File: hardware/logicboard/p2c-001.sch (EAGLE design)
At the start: 45 parts, among them IC1 74LS07N, K1 G5V1, T1 2SC1815

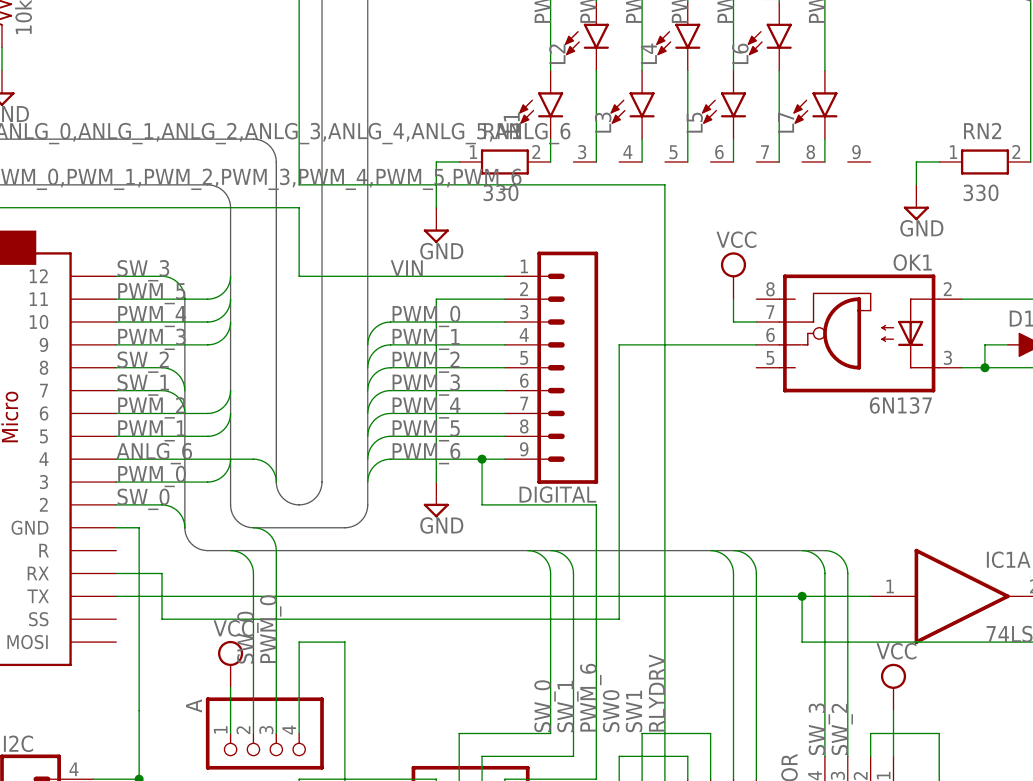
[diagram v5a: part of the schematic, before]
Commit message: Added RCV LED.
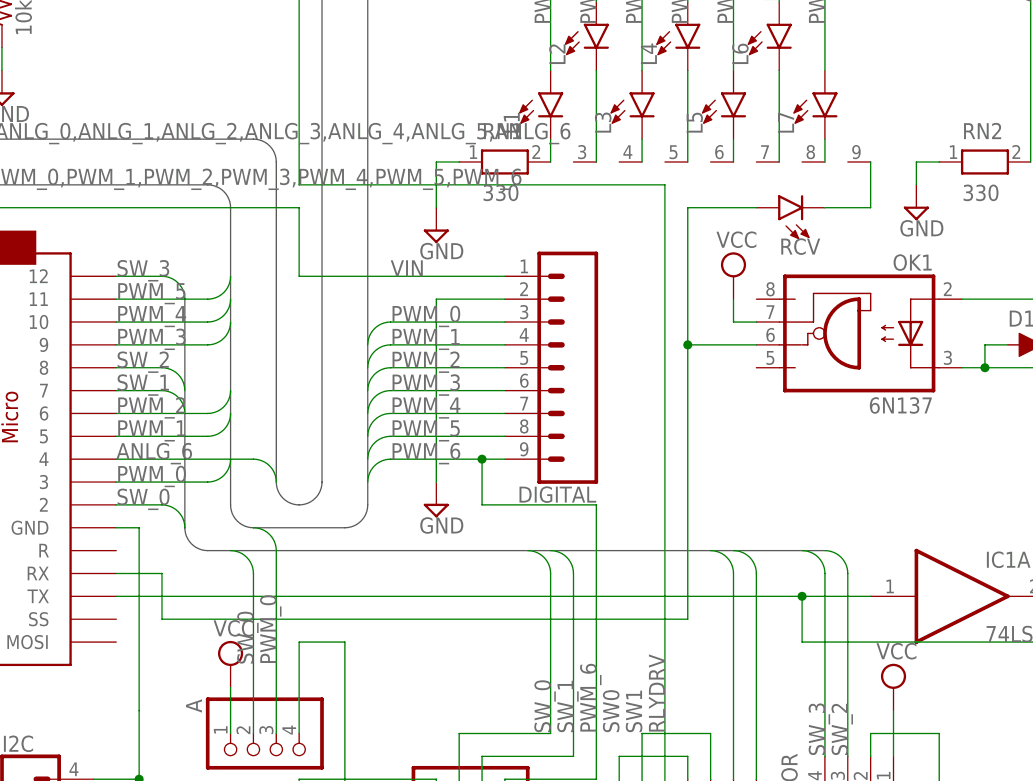
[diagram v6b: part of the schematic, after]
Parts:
- added RCV: (no value), SparkFun-LED:LED-3MM-NO_SILK
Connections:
- new net N$1: RCV.C, RN1.9
- net MIDIIN: now also RCV.A
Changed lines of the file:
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@@
 <part name="XOUT" library="SparkFun-Connectors" library_urn="urn:adsk.eagle:library:513" deviceset="CONN_05" device="" package3d_urn="urn:adsk.eagle:package:38104/1"/>
 <part name="U$3" library="pineapple" deviceset="KANAYA768_SILK" device=""/>
+<part name="RCV" library="SparkFun-LED" deviceset="LED" device="-3MM-NO_SILK"/>
 </parts>
 <sheets>
@@
 <instance part="XOUT" gate="G$1" x="236.22" y="111.76" rot="MR180"/>
 <instance part="U$3" gate="G$1" x="187.96" y="5.08"/>
+<instance part="RCV" gate="G$1" x="142.24" y="99.06" rot="R90"/>
 </instances>
 <busses>
@@
 <segment>
 <pinref part="OK1" gate="A" pin="VO"/>
-<wire x1="139.7" y1="83.82" x2="124.46" y2="83.82" width="0.1524" layer="91"/>
+<wire x1="139.7" y1="83.82" x2="132.08" y2="83.82" width="0.1524" layer="91"/>
 <pinref part="U$2" gate="G$1" pin="RX"/>
-<wire x1="124.46" y1="83.82" x2="124.46" y2="53.34" width="0.1524" layer="91"/>
-<wire x1="124.46" y1="53.34" x2="73.66" y2="53.34" width="0.1524" layer="91"/>
+<wire x1="132.08" y1="83.82" x2="132.08" y2="53.34" width="0.1524" layer="91"/>
+<wire x1="132.08" y1="53.34" x2="73.66" y2="53.34" width="0.1524" layer="91"/>
 <wire x1="73.66" y1="53.34" x2="73.66" y2="58.42" width="0.1524" layer="91"/>
 <wire x1="73.66" y1="58.42" x2="68.58" y2="58.42" width="0.1524" layer="91"/>
+<wire x1="132.08" y1="99.06" x2="132.08" y2="83.82" width="0.1524" layer="91"/>
+<junction x="132.08" y="83.82"/>
+<pinref part="RCV" gate="G$1" pin="A"/>
+<wire x1="139.7" y1="99.06" x2="132.08" y2="99.06" width="0.1524" layer="91"/>
 </segment>
 </net>
@@
 </segment>
 </net>
+<net name="N$1" class="0">
+<segment>
+<pinref part="RN1" gate="1" pin="9"/>
+<wire x1="152.4" y1="104.14" x2="152.4" y2="99.06" width="0.1524" layer="91"/>
+<pinref part="RCV" gate="G$1" pin="C"/>
+<wire x1="152.4" y1="99.06" x2="147.32" y2="99.06" width="0.1524" layer="91"/>
+</segment>
+</net>
